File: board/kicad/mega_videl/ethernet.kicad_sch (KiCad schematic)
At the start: 27 parts, among them U14 LAN9220-ABZJ, Y3 25MHz

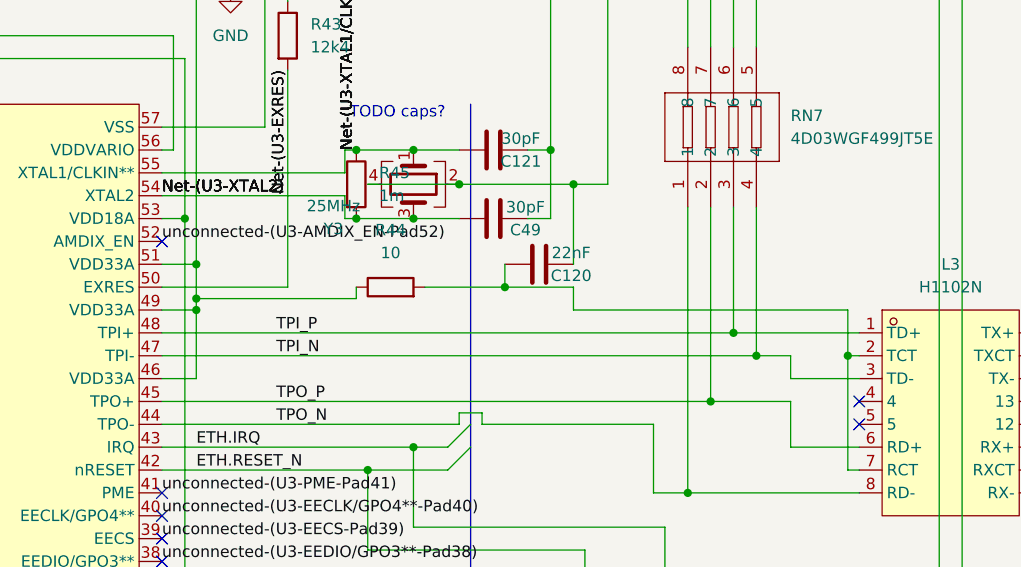
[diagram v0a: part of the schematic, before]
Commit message: Made board narrower so it fits next to CT60 SDRAM. Moved JTAG over slightly - more height
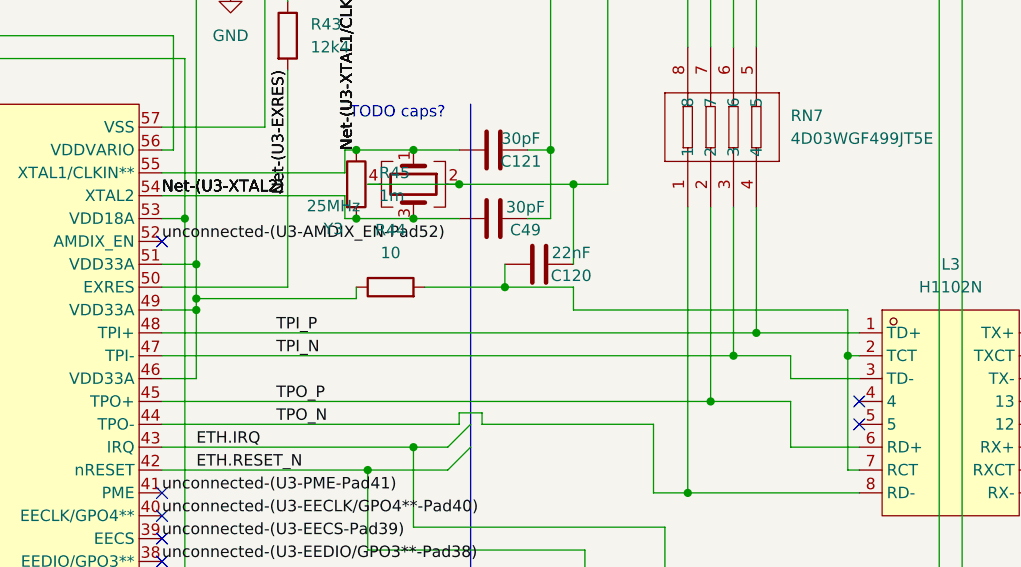
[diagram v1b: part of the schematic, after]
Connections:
- net TPI_N: now also RN7.3; no longer RN7.4
- net TPI_P: now also RN7.4; no longer RN7.3
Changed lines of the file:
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@@
-	)
-	(junction
-		(at 234.95 67.31)
-		(diameter 0)
-		(color 0 0 0 0)
 	)
 	(junction
@@
 	)
 	(junction
-		(at 237.49 69.85)
-		(diameter 0)
-		(color 0 0 0 0)
-	)
-	(junction
 		(at 204.47 50.8)
 		(diameter 0)
@@
 	)
 	(junction
+		(at 234.95 69.85)
+		(diameter 0)
+		(color 0 0 0 0)
+	)
+	(junction
 		(at 238.76 146.05)
 		(diameter 0)
@@
 	(junction
 		(at 232.41 74.93)
+		(diameter 0)
+		(color 0 0 0 0)
+	)
+	(junction
+		(at 237.49 67.31)
 		(diameter 0)
 		(color 0 0 0 0)
@@
 	(wire
 		(pts
-			(xy 171.45 67.31) (xy 234.95 67.31)
+			(xy 171.45 67.31) (xy 237.49 67.31)
 		)
 		(stroke
@@
 		)
 	)
-	(wire
-		(pts
-			(xy 171.45 69.85) (xy 237.49 69.85)
-		)
-		(stroke
-			(width 0)
-			(type default)
-		)
-	)
 	(bus
 		(pts
@@
 	(wire
 		(pts
-			(xy 234.95 53.34) (xy 234.95 67.31)
-		)
-		(stroke
-			(width 0)
-			(type default)
-		)
-	)
-	(wire
-		(pts
 			(xy 118.11 52.07) (xy 105.41 52.07)
 		)
@@
 	(wire
 		(pts
-			(xy 247.65 64.77) (xy 217.17 64.77)
+			(xy 217.17 64.77) (xy 247.65 64.77)
 		)
 		(stroke
@@
 	(wire
 		(pts
+			(xy 234.95 53.34) (xy 234.95 69.85)
+		)
+		(stroke
+			(width 0)
+			(type default)
+		)
+	)
+	(wire
+		(pts
 			(xy 229.87 135.89) (xy 260.35 135.89)
 		)
@@
 	(wire
 		(pts
-			(xy 234.95 67.31) (xy 248.92 67.31)
-		)
-		(stroke
-			(width 0)
-			(type default)
-		)
-	)
-	(wire
-		(pts
 			(xy 207.01 76.2) (xy 207.01 77.47)
 		)
@@
 	(wire
 		(pts
+			(xy 237.49 67.31) (xy 248.92 67.31)
+		)
+		(stroke
+			(width 0)
+			(type default)
+		)
+	)
+	(wire
+		(pts
 			(xy 90.17 59.69) (xy 118.11 59.69)
 		)
@@
 	(wire
 		(pts
-			(xy 237.49 53.34) (xy 237.49 69.85)
-		)
-		(stroke
-			(width 0)
-			(type default)
-		)
-	)
-	(wire
-		(pts
 			(xy 185.42 26.67) (xy 182.88 26.67)
 		)
@@
 	(wire
 		(pts
+			(xy 237.49 53.34) (xy 237.49 67.31)
+		)
+		(stroke
+			(width 0)
+			(type default)
+		)
+	)
+	(wire
+		(pts
 			(xy 118.11 90.17) (xy 110.49 90.17)
 		)
@@
 	(wire
 		(pts
+			(xy 234.95 69.85) (xy 241.3 69.85)
+		)
+		(stroke
+			(width 0)
+			(type default)
+		)
+	)
+	(wire
+		(pts
 			(xy 194.31 91.44) (xy 194.31 82.55)
 		)
@@
 	(wire
 		(pts
-			(xy 237.49 69.85) (xy 241.3 69.85)
-		)
-		(stroke
+			(xy 171.45 69.85) (xy 234.95 69.85)
+		)
+		(stroke

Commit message: Reviewed and fixed many issues. e.g. missing decoupling for 1.35v under fpga
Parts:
- added C134: 4.7uF, Capacitor_SMD:C_0805_2012Metric, symbol Device:C
- R56: renamed from R45; value 1m -> 1M
- renumbered C106 to C117, C107 to C118, C108 to C119, C109 to C123, C110 to C124, C112 to C126, C113 to C127, C115 to C129, C117 to C131, C120 to C135, C121 to C136, C122 to C137, C48 to C47, C49 to C48, R23 to R27, R24 to R29, R46 to R52, R43 to R53, R44 to R54, R47 to R55, U14 to U15
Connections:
- net +3V3: now also FPC1.10
- net +3V3A_ETH: now also C134.1; no longer FPC1.10
- net GND: now also C134.2
- net +1V8 renamed +1V8_ETH
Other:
- moved on the sheet: C129

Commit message: Assigned all parts with JLCPCB plugin
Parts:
- C117, C118, C119, C126, C129, C131, C47: LCSC (none) -> C1525
- C123, C134: LCSC (none) -> C1779
- C124, C127: value 0.01uF -> 10nF; LCSC (none) -> C15195
- C135: LCSC (none) -> C21122
- C136, C48: LCSC (none) -> C1658
- C137: LCSC (none) -> C9196
- FB4: LCSC (none) -> C85840
- R27, R29: LCSC (none) -> C23162
- R52, R55: LCSC (none) -> C4275
- R53: LCSC (none) -> C137798
- R54: LCSC (none) -> C22859
- R56: LCSC (none) -> C22935
- Y3: LCSC (none) -> C5308007

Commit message: Added series resistors to all CT lines. They ring up to 7V apparently according to Super Videl devs. Some of that is likely the length of scope lines. The safety fix here is to add small 33ohm resistors and to enable clamp diodes in the FPGA core.
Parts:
- renumbered R52 to R138, R53 to R139, R54 to R140, R55 to R141, R56 to R142, R27 to R46, R29 to R48
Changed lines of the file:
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@@
 		(in_pos_files yes)
 		(dnp no)
-		(property "Reference" "R52"
+		(property "Reference" "R138"
 			(at 277.622 101.6 0)
 			(show_name no)
@@
 			(project "mega_videl"
 				(path "/10511203-7d65-4cdf-a1a4-c07b44ea87e2/796433b4-41c0-47e1-bce3-aa98af267221"
-					(reference "R52")
+					(reference "R138")
 					(unit 1)
 				)
@@
 		(dnp no)
 		(fields_autoplaced yes)
-		(property "Reference" "R53"
+		(property "Reference" "R139"
 			(at 187.96 33.0199 0)
 			(show_name no)
@@
 			(project "mega_videl"
 				(path "/10511203-7d65-4cdf-a1a4-c07b44ea87e2/796433b4-41c0-47e1-bce3-aa98af267221"
-					(reference "R53")
+					(reference "R139")
 					(unit 1)
 				)
@@
 		(dnp no)
 		(fields_autoplaced yes)
-		(property "Reference" "R56"
+		(property "Reference" "R142"
 			(at 195.58 49.5299 0)
 			(show_name no)
@@
 			(project "mega_videl"
 				(path "/10511203-7d65-4cdf-a1a4-c07b44ea87e2/796433b4-41c0-47e1-bce3-aa98af267221"
-					(reference "R56")
+					(reference "R142")
 					(unit 1)
 				)
@@
 		(dnp no)
 		(fields_autoplaced yes)
-		(property "Reference" "R54"
+		(property "Reference" "R140"
 			(at 196.85 55.88 90)
 			(show_name no)
@@
 			(project "mega_videl"
 				(path "/10511203-7d65-4cdf-a1a4-c07b44ea87e2/796433b4-41c0-47e1-bce3-aa98af267221"
-					(reference "R54")
+					(reference "R140")
 					(unit 1)
 				)
@@
 		(dnp no)
 		(fields_autoplaced yes)
-		(property "Reference" "R29"
+		(property "Reference" "R48"
 			(at 229.87 96.5199 0)
 			(show_name no)
@@
 			(project "mega_videl"
 				(path "/10511203-7d65-4cdf-a1a4-c07b44ea87e2/796433b4-41c0-47e1-bce3-aa98af267221"
-					(reference "R29")
+					(reference "R48")
 					(unit 1)
 				)
@@
 		(in_pos_files yes)
 		(dnp no)
-		(property "Reference" "R55"
+		(property "Reference" "R141"
 			(at 267.97 102.362 0)
 			(show_name no)
@@
 			(project "mega_videl"
 				(path "/10511203-7d65-4cdf-a1a4-c07b44ea87e2/796433b4-41c0-47e1-bce3-aa98af267221"
-					(reference "R55")
+					(reference "R141")
 					(unit 1)
 				)
@@
 		(dnp no)
 		(fields_autoplaced yes)
-		(property "Reference" "R27"
+		(property "Reference" "R46"
 			(at 220.98 96.5199 0)
 			(show_name no)
@@
 			(project "mega_videl"
 				(path "/10511203-7d65-4cdf-a1a4-c07b44ea87e2/796433b4-41c0-47e1-bce3-aa98af267221"
-					(reference "R27")
+					(reference "R46")
 					(unit 1)
 				)
